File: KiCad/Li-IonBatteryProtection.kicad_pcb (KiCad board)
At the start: 2 copper layers, 179.1 x 54.6 mm, 55 parts, among them J1 CONN_02X03, J2 CONN_01X02, Q1 IRF540N, Q2 2N2222A, Q3 2N2222A, Q4 2N2222A, Q5 2N2222A, Q6 2N2222A, U1 LM311N, U2 PC817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

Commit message: Updated to the PCB.
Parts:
- moved C4 3.81 mm to (205.7, 109.2)
- moved Q1 1.27 mm to (218.4, 118.1)
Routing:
- net Net-(C4-Pad1): track 45.7 -> 55.9 mm, vias 2 -> 3
- net Battery-GND: track 363.6 -> 361.4 mm
- net Battery-4: track 137.5 -> 135.7 mm
- net Net-(C3-Pad2): track 49.3 -> 48.0 mm
- added copper zone on B.Cu, net (none)
- added copper zone on F.Cu, net (none)
- removed copper zone on B.Cu, net Battery-4
- removed copper zone on F.Cu, net Battery-4
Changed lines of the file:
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@@
     (thickness 1.6)
     (drawings 4)
-    (tracks 291)
+    (tracks 294)
     (zones 0)
     (modules 55)
@@
   )
   (module Capacitors_ThroughHole:C_Radial_D5_L11_P2.5 (layer F.Cu)
-    (at 209.55 109.22 180)
+    (at 205.74 109.22 180)
     (descr "Radial Electrolytic Capacitor Diameter 5mm x Length 11mm, Pitch 2.5mm")
     (tags "Electrolytic Capacitor")
@@
   )
   (module TO_SOT_Packages_THT:TO-220_Neutral123_Horizontal (layer F.Cu)
-    (at 219.71 118.11)
+    (at 218.44 118.11)
     (descr "TO-220, Neutral, Horizontal,")
     (tags "TO-220, Neutral, Horizontal,")
@@
   (gr_line (start 231.14 72.39) (end 231.14 127) (angle 90) (layer Edge.Cuts) (width 0.15))
   (gr_line (start 52.07 72.39) (end 231 72.39) (angle 90) (layer Edge.Cuts) (width 0.15))
-  (segment (start 209.55 109.22) (end 219.71 109.22) (width 0.5) (layer F.Cu) (net 1) (status 10))
-  (segment (start 219.71 109.22) (end 219.71 118.11) (width 0.5) (layer F.Cu) (net 1))
-  (segment (start 209.55 82.55) (end 209.55 88.9) (width 0.5) (layer F.Cu) (net 1))
-  (segment (start 209.55 92.71) (end 209.55 109.22) (width 0.5) (layer F.Cu) (net 1) (status 20))
+  (segment (start 218.44 118.11) (end 218.44 121.92) (width 0.5) (layer B.Cu) (net 1))
+  (via (at 209.55 109.22) (size 0.6) (drill 0.4) (layers F.Cu B.Cu) (net 1))
+  (segment (start 209.55 121.92) (end 209.55 109.22) (width 0.5) (layer B.Cu) (net 1))
+  (segment (start 218.44 121.92) (end 209.55 121.92) (width 0.5) (layer B.Cu) (net 1))
+  (segment (start 209.55 109.22) (end 209.55 92.71) (width 0.5) (layer F.Cu) (net 1))
+  (via (at 209.55 88.9) (size 0.6) (drill 0.4) (layers F.Cu B.Cu) (net 1))
+  (segment (start 209.55 88.9) (end 209.55 92.71) (width 0.5) (layer B.Cu) (net 1))
   (via (at 209.55 92.71) (size 0.6) (drill 0.4) (layers F.Cu B.Cu) (net 1))
-  (segment (start 209.55 88.9) (end 209.55 92.71) (width 0.5) (layer B.Cu) (net 1))
-  (via (at 209.55 88.9) (size 0.6) (drill 0.4) (layers F.Cu B.Cu) (net 1))
-  (segment (start 207.05 109.22) (end 206.502 109.474) (width 0.25) (layer B.Cu) (net 2) (status 80030))
-  (segment (start 206.502 109.474) (end 199.39 116.84) (width 0.25) (layer B.Cu) (net 2) (status 80010))
+  (segment (start 209.55 88.9) (end 209.55 82.55) (width 0.5) (layer F.Cu) (net 1))
+  (segment (start 205.74 109.22) (end 209.55 109.22) (width 0.5) (layer F.Cu) (net 1) (status 10))
+  (segment (start 203.24 109.22) (end 202.692 109.474) (width 0.25) (layer B.Cu) (net 2) (status 80030))
+  (segment (start 202.692 109.474) (end 199.39 116.84) (width 0.25) (layer B.Cu) (net 2) (status 80010))
   (segment (start 199.39 116.84) (end 199.39 118.11) (width 0.25) (layer B.Cu) (net 2) (status 80000))
   (segment (start 199.39 118.11) (end 201.93 120.65) (width 0.25) (layer B.Cu) (net 2) (status 80000))
@@
   (segment (start 172.72 77.47) (end 177.8 82.55) (width 0.25) (layer F.Cu) (net 2))
   (segment (start 190.5 121.84) (end 195.5 121.84) (width 0.25) (layer F.Cu) (net 2))
-  (segment (start 222.25 124.46) (end 222.25 118.11) (width 0.25) (layer F.Cu) (net 2))
+  (segment (start 220.98 124.46) (end 220.98 118.11) (width 0.25) (layer F.Cu) (net 2) (status 20))
   (segment (start 195.58 124.46) (end 201.93 124.46) (width 0.25) (layer F.Cu) (net 2))
-  (segment (start 201.93 124.46) (end 222.25 124.46) (width 0.25) (layer F.Cu) (net 2))
+  (segment (start 201.93 124.46) (end 220.98 124.46) (width 0.25) (layer F.Cu) (net 2))
   (segment (start 195.58 121.92) (end 195.58 124.46) (width 0.25) (layer F.Cu) (net 2))
   (segment (start 195.5 121.84) (end 195.58 121.92) (width 0.25) (layer F.Cu) (net 2))
@@
   (segment (start 227.33 86.36) (end 227.33 97.79) (width 0.5) (layer F.Cu) (net 2))
   (segment (start 227.33 97.79) (end 227.33 118.11) (width 0.5) (layer F.Cu) (net 2))
-  (segment (start 227.33 118.11) (end 222.25 118.11) (width 0.5) (layer F.Cu) (net 2))
+  (segment (start 227.33 118.11) (end 220.98 118.11) (width 0.5) (layer F.Cu) (net 2) (status 20))
   (segment (start 196.85 97.79) (end 196.85 101.6) (width 0.25) (layer F.Cu) (net 3))
-  (segment (start 201.93 118.11) (end 217.17 118.11) (width 0.25) (layer F.Cu) (net 3) (status 10))
+  (segment (start 201.93 118.11) (end 215.9 118.11) (width 0.25) (layer F.Cu) (net 3) (status 20))
   (segment (start 191.69 101.6) (end 196.85 101.6) (width 0.25) (layer F.Cu) (net 3) (status 10))
   (segment (start 198.12 114.3) (end 201.93 118.11) (width 0.25) (layer F.Cu) (net 3) (status 20))
@@
   (segment (start 223.52 82.55) (end 226.06 82.55) (width 0.5) (layer F.Cu) (net 6))
   (segment (start 226.06 82.55) (end 226.06 76.2) (width 0.5) (layer F.Cu) (net 6))
-  (segment (start 226.06 76.2) (end 224.79 74.93) (width 0.5) (layer F.Cu) (net 6))
-  (segment (start 224.79 74.93) (end 204.47 74.93) (width 0.5) (layer F.Cu) (net 6))
-  (segment (start 204.47 74.93) (end 204.55 75.01) (width 0.5) (layer F.Cu) (net 6))
-  (segment (start 204.55 75.01) (end 204.55 82.55) (width 0.5) (layer F.Cu) (net 6) (status 20))
+  (segment (start 226.06 76.2) (end 224.79 76.2) (width 0.5) (layer F.Cu) (net 6))
+  (segment (start 224.79 76.2) (end 204.47 76.2) (width 0.5) (layer F.Cu) (net 6))
+  (segment (start 204.47 76.2) (end 204.55 76.28) (width 0.5) (layer F.Cu) (net 6))
+  (segment (start 204.55 76.28) (end 204.55 82.55) (width 0.5) (layer F.Cu) (net 6) (status 20))
   (segment (start 177.8 113.03) (end 177.8 109.22) (width 0.25) (layer B.Cu) (net 6))
   (segment (start 185.42 101.6) (end 186.69 101.6) (width 0.25) (layer B.Cu) (net 6))
@@
   (segment (start 138.43 113.03) (end 146.05 120.65) (width 0.25) (layer B.Cu) (net 37))
   (segment (start 170.18 113.03) (end 177.8 120.65) (width 0.25) (layer B.Cu) (net 38))
-  (zone (net 6) (net_name Battery-4) (layer F.Cu) (hatch edge 0.508)
+  (zone (net 0) (net_name "") (layer B.Cu) (hatch edge 0.508)
     (connect_pads (clearance 0.508))
     (min_thickness 0.254)
@@
     (polygon
       (pts
-        (xy 226.06 115.57) (xy 213.36 115.57) (xy 208.28 110.49) (xy 208.28 96.52) (xy 226.06 96.52)
-        (xy 226.06 115.57)
+        (xy 226.06 115.57) (xy 210.82 115.57) (xy 210.82 95.25) (xy 226.06 95.25) (xy 226.06 115.57)
       )
     )
   )
-  (zone (net 6) (net_name Battery-4) (layer B.Cu) (hatch edge 0.508)
+  (zone (net 0) (net_name "") (layer F.Cu) (hatch edge 0.508)
     (connect_pads (clearance 0.508))
     (min_thickness 0.254)
@@
     (polygon
       (pts
-        (xy 226.06 115.57) (xy 213.36 115.57) (xy 208.28 110.49) (xy 208.28 96.52) (xy 226.06 96.52)
-        (xy 226.06 115.57)
+        (xy 226.06 115.57) (xy 210.82 115.57) (xy 210.82 95.25) (xy 226.06 95.25) (xy 226.06 115.57)
       )
     )

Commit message: Hopefully finished the PCB.
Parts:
- moved R2 41.4 mm to (98.4, 95.2)
- moved R7 40.1 mm to (97.2, 85.1)
- moved R5 40.0 mm to (97.2, 90.2)
- moved R3 39.4 mm to (104.1, 120.7)
- moved R4 36.9 mm to (110.5, 96.5)
- moved R1 36.5 mm to (103.5, 100.3), turned to 270 degrees
- moved U2 35.9 mm to (110.5, 85.1)
- moved Q3 35.1 mm to (116.2, 94.0)
- moved R6 35.0 mm to (116.2, 99.1)
- moved R9 34.4 mm to (123.2, 95.2)
- moved U1 34.3 mm to (109.2, 114.3)
- moved R14 33.1 mm to (121.9, 85.1)
- moved R12 33.0 mm to (121.9, 90.2)
- moved R10 32.4 mm to (128.9, 120.7)
- moved D1 32.4 mm to (99.1, 106.7), turned to 270 degrees
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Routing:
- net Battery-GND: track 361.4 -> 304.7 mm
- net Battery-1: track 232.2 -> 196.5 mm, vias 1 -> 0
- net Battery-2: track 202.1 -> 167.5 mm
- net Battery-3: track 192.9 -> 158.4 mm
- net Net-(C1-Pad1): track 160.0 -> 138.4 mm
- net Battery-4: track 135.7 -> 120.9 mm
- net Net-(C3-Pad2): track 48.0 -> 35.4 mm
- net Net-(R14-Pad2): track 8.67 -> 3.17 mm
- net Net-(R28-Pad2): track 8.67 -> 3.17 mm
- net Net-(R7-Pad2): track 8.67 -> 3.17 mm
- net Net-(R21-Pad2): track 8.67 -> 3.18 mm
- net Net-(C4-Pad1): track 55.9 -> 50.8 mm, vias 3 -> 1
- net Net-(C2-Pad1): track 20.1 -> 15.2 mm
- net Net-(R4-Pad1): track 36.8 -> 33.0 mm
- net Net-(R11-Pad1): track 36.8 -> 33.1 mm
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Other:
- board size 179.1 x 54.6 mm -> 137.1 x 47 mm

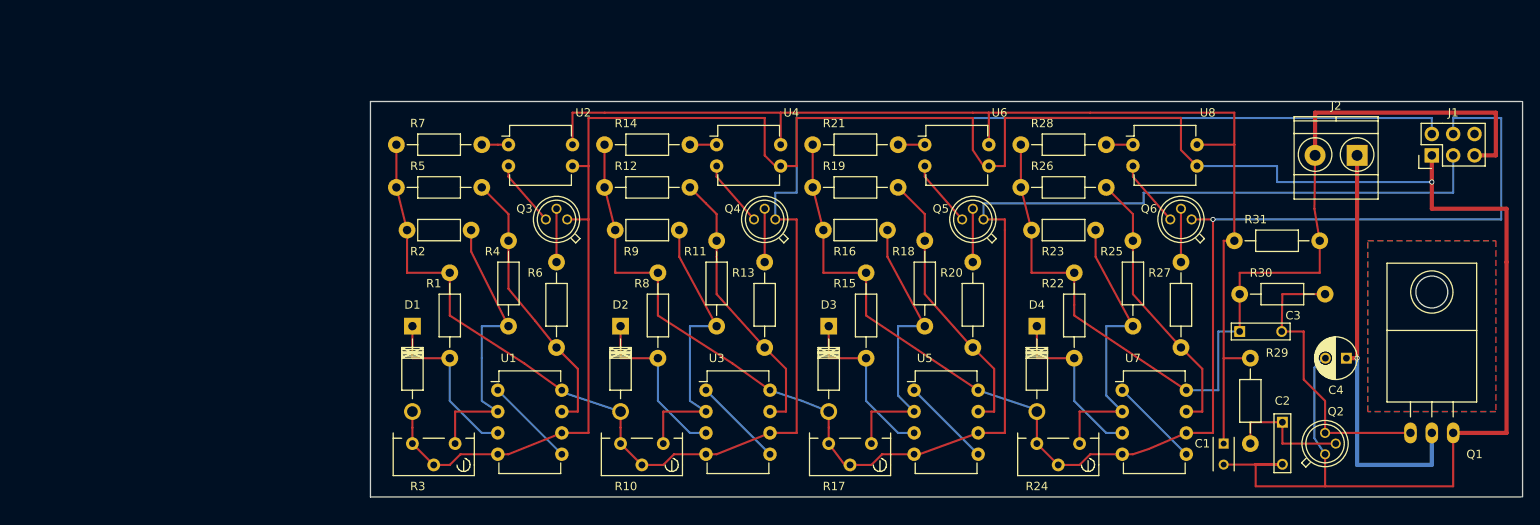
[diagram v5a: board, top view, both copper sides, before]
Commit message: Added test points to the schematic.
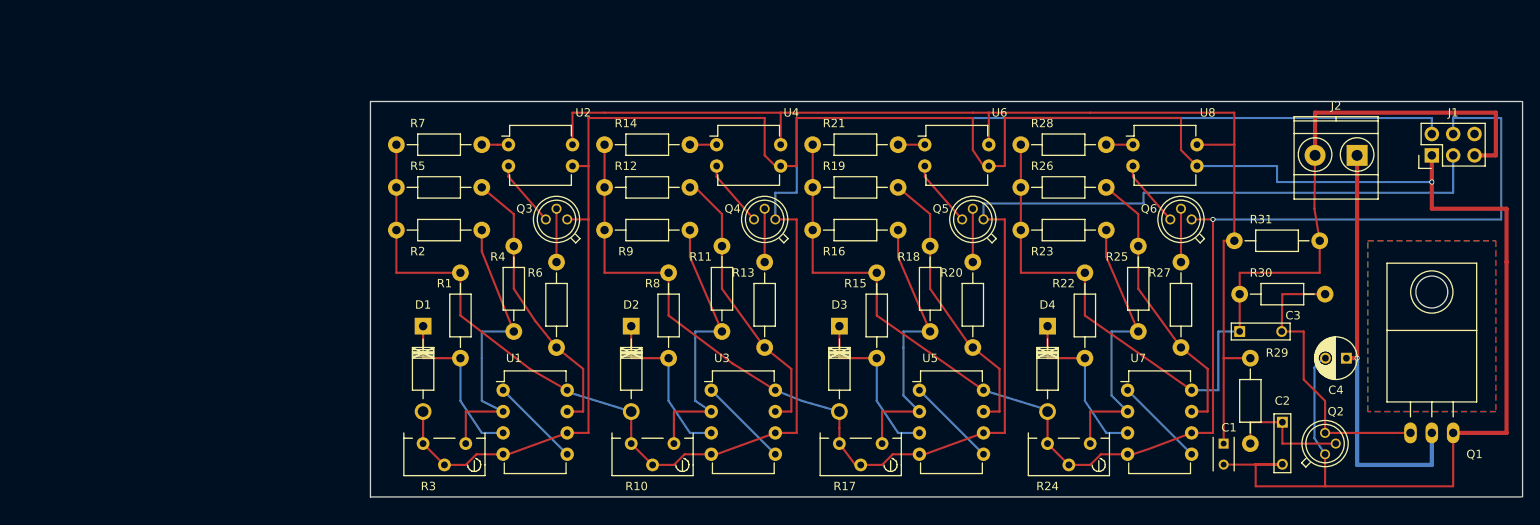
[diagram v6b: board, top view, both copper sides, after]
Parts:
- R16, R2, R23, R9: footprint Resistors_ThroughHole:Resistor_Horizontal_RM7mm -> Resistors_ThroughHole:Resistor_Horizontal_RM10mm
- moved D3 1.27 mm to (149.9, 106.7)
- moved D4 1.27 mm to (174.6, 106.7)
- moved R1 1.27 mm to (104.8, 100.3)
- moved R10 1.27 mm to (130.2, 120.7)
- moved R15 1.27 mm to (154.3, 100.3)
- moved R16 1.27 mm to (146.7, 95.2)
- moved R17 1.27 mm to (154.9, 120.7)
- moved R23 1.27 mm to (171.4, 95.2)
- moved R24 1.27 mm to (179.7, 120.7)
- moved D1 1.27 mm to (100.3, 106.7)
- moved D2 1.27 mm to (125.1, 106.7)
- moved R2 1.27 mm to (97.2, 95.2)
- moved R3 1.27 mm to (105.4, 120.7)
- moved R9 1.27 mm to (121.9, 95.2)
- moved R22 1.27 mm to (179.1, 100.3)
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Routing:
- net Battery-GND: track 304.7 -> 303.4 mm
- net Battery-4: track 120.9 -> 122.2 mm
- net Battery-2: track 167.5 -> 168.7 mm
- net Battery-1: track 196.5 -> 197.6 mm
- net Battery-3: track 158.4 -> 159.5 mm
- net Net-(R16-Pad2): track 35.6 -> 34.6 mm
- net Net-(R10-Pad1): track 35.8 -> 34.8 mm
- net Net-(R23-Pad2): track 35.6 -> 34.6 mm
- net Net-(R11-Pad1): track 33.1 -> 33.7 mm
- net Net-(R4-Pad1): track 33.0 -> 33.5 mm

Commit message: Updated the source files.
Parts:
- added REF**: 1pin, Connect:1pin, F.Cu at (64.8, 74.3)
- added REF**: Measurement_Point_Square-TH_Small, Measurement_Points:Measurement_Point_Square-TH_Small, F.Cu at (196.8, 101.6)
- added REF**: Measurement_Point_Square-TH_Small, Measurement_Points:Measurement_Point_Square-TH_Small, F.Cu at (184.2, 101.6)
- added REF**: Measurement_Point_Square-TH_Small, Measurement_Points:Measurement_Point_Square-TH_Small, F.Cu at (190.5, 92.7)
- added REF**: 1pin, Connect:1pin, F.Cu at (64.8, 123.8)
- added REF**: 1pin, Connect:1pin, F.Cu at (203.2, 74.3)
- added REF**: 1pin, Connect:1pin, F.Cu at (203.2, 123.8)
- added REF**: 1pin, Connect:1pin, F.Cu at (143.5, 96.5)
- added REF**: Measurement_Point_Square-TH_Small, Measurement_Points:Measurement_Point_Square-TH_Small, F.Cu at (184.2, 92.7)
- added REF**: Measurement_Point_Square-TH_Small, Measurement_Points:Measurement_Point_Square-TH_Small, F.Cu at (196.8, 92.7)
- added REF**: Measurement_Point_Square-TH_Small, Measurement_Points:Measurement_Point_Square-TH_Small, F.Cu at (184.2, 110.5)
- added REF**: Measurement_Point_Square-TH_Small, Measurement_Points:Measurement_Point_Square-TH_Small, F.Cu at (196.8, 110.5)
- added TP1: TEST_1P, Measurement_Points:Measurement_Point_Round-TH_Big, F.Cu at (66.7, 115.6)
- added TP10: TEST_1P, Measurement_Points:Measurement_Point_Round-TH_Small, F.Cu at (167.0, 80.0)
- added TP11: TEST_1P, Measurement_Points:Measurement_Point_Round-TH_Small, F.Cu at (176.5, 101.0)
- added TP2: TEST_1P, Measurement_Points:Measurement_Point_Round-TH_Big, F.Cu at (91.4, 115.6)
- added TP3: TEST_1P, Measurement_Points:Measurement_Point_Round-TH_Big, F.Cu at (116.2, 115.6)
- added TP4: TEST_1P, Measurement_Points:Measurement_Point_Round-TH_Big, F.Cu at (141.0, 115.6)
- added TP5: TEST_1P, Measurement_Points:Measurement_Point_Round-TH_Small, F.Cu at (171.4, 80.0)
- added TP6: TEST_1P, Measurement_Points:Measurement_Point_Round-TH_Big, F.Cu at (89.5, 104.1)
- added TP7: TEST_1P, Measurement_Points:Measurement_Point_Round-TH_Small, F.Cu at (114.3, 104.1)
- added TP8: TEST_1P, Measurement_Points:Measurement_Point_Round-TH_Small, F.Cu at (139.1, 104.1)
- added TP9: TEST_1P, Measurement_Points:Measurement_Point_Round-TH_Big, F.Cu at (163.2, 104.1)
- added W5: TEST_1P, Measurement_Points:Measurement_Point_Round-TH_Big, F.Cu at (172.1, 78.7)
- added W7: TEST_1P, Measurement_Points:Measurement_Point_Round-TH_Big, F.Cu at (116.8, 104.1)
- added W8: TEST_1P, Measurement_Points:Measurement_Point_Round-TH_Big, F.Cu at (141.6, 104.1)
- moved C3 30.3 mm to (167.6, 102.2)
- moved Q5 30.3 mm to (135.9, 88.9)
- moved R20 30.3 mm to (135.9, 94.0)
- moved D3 30.3 mm to (120.0, 101.6)
- moved R10 30.3 mm to (100.3, 115.6)
- moved R15 30.3 mm to (124.5, 95.2)
- moved C1 30.3 mm to (165.7, 115.6)
- moved D1 30.3 mm to (70.5, 101.6)
- moved D2 30.3 mm to (95.2, 101.6)
- moved D4 30.3 mm to (144.8, 101.6)
- moved Q2 30.3 mm to (177.8, 115.6)
- moved R17 30.3 mm to (125.1, 115.6)
- moved R24 30.3 mm to (149.9, 115.6)
- moved R29 30.3 mm to (168.9, 115.6)
- moved R3 30.3 mm to (75.6, 115.6)
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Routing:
- net Battery-4: track 122.2 -> 127.6 mm
- net Battery-GND: track 303.4 -> 308.3 mm
- net Battery-2: track 168.7 -> 173.5 mm
- net Battery-1: track 197.6 -> 202.5 mm
- net Battery-3: track 159.5 -> 163.9 mm
- net Net-(C3-Pad2): track 35.4 -> 39.1 mm
- net Net-(R18-Pad1): track 33.5 -> 36.7 mm
- net Net-(R4-Pad1): track 33.5 -> 36.7 mm
- net Net-(R11-Pad1): track 33.7 -> 36.9 mm
- net Net-(R25-Pad1): track 33.5 -> 36.1 mm
- added copper zone on B.Cu, net Battery-GND
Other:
- board size 137.1 x 47 mm -> 147.2 x 58.3 mm
